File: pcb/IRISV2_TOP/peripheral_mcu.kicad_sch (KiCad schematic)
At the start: 30 parts, among them IC2 S25FL256LAGNFI010, IC3 STM32C552MET6, J6 Conn_02x04_Top_Bottom, Y3 24mHz 8pf, Y4 32.768kHz 12.5pF

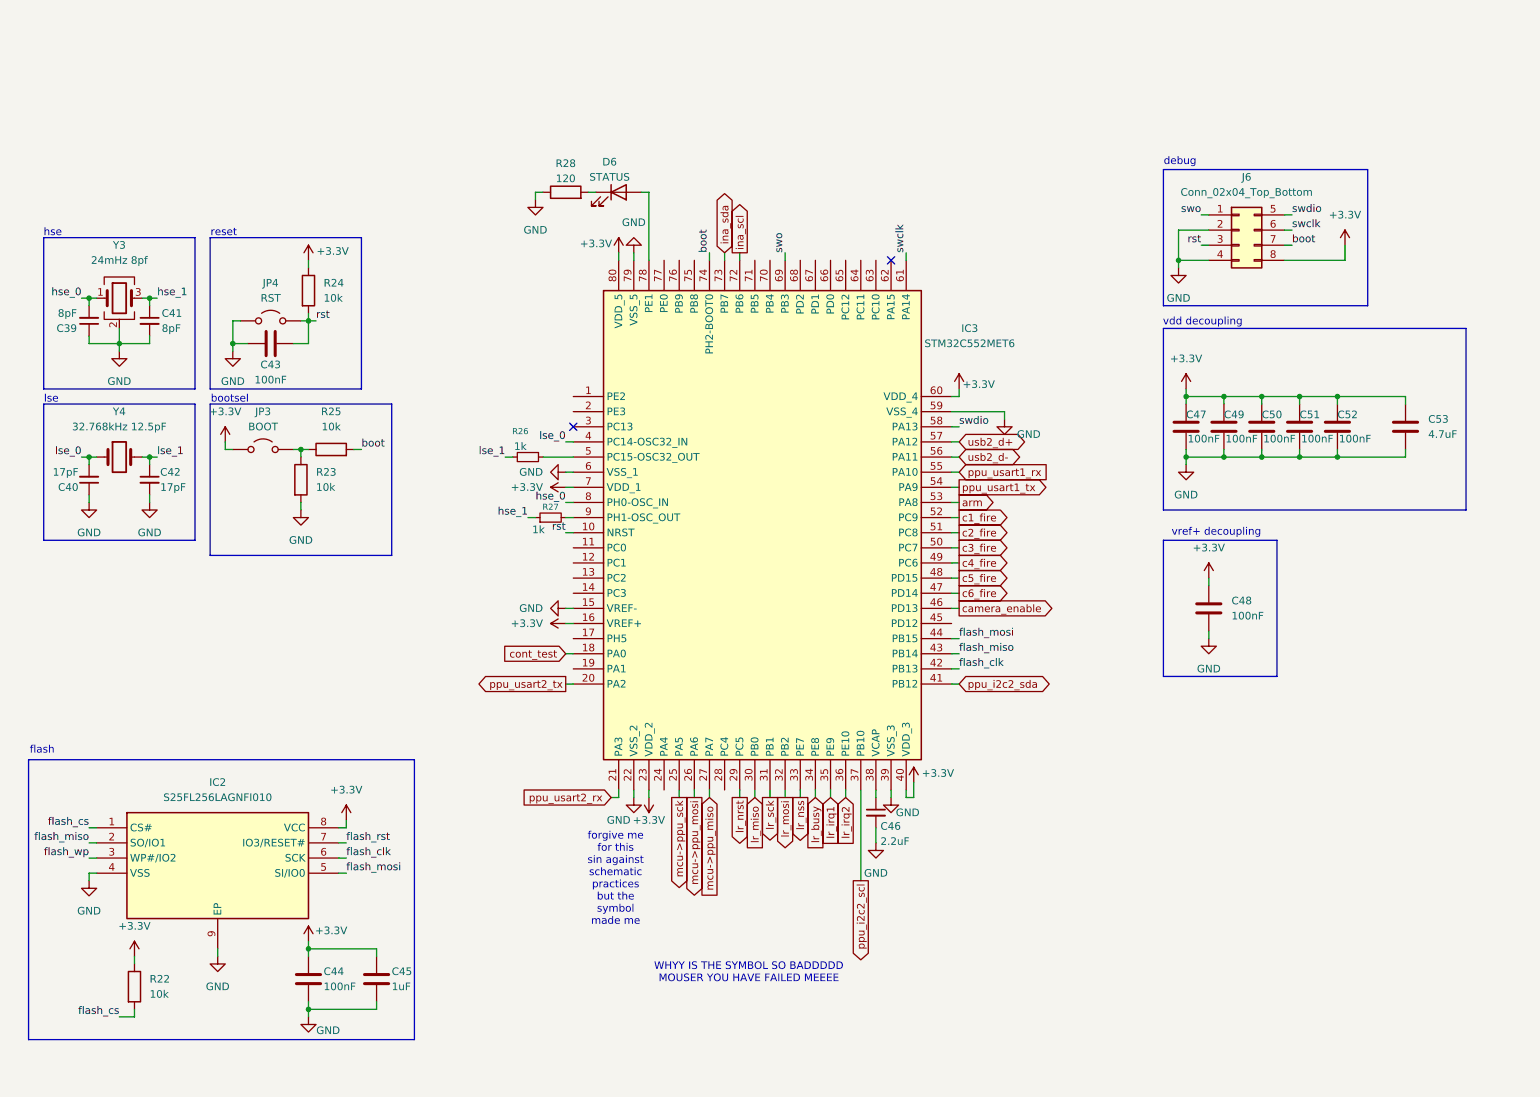
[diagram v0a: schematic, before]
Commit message: split into subprojects, fixed up stuff, started real pcb work
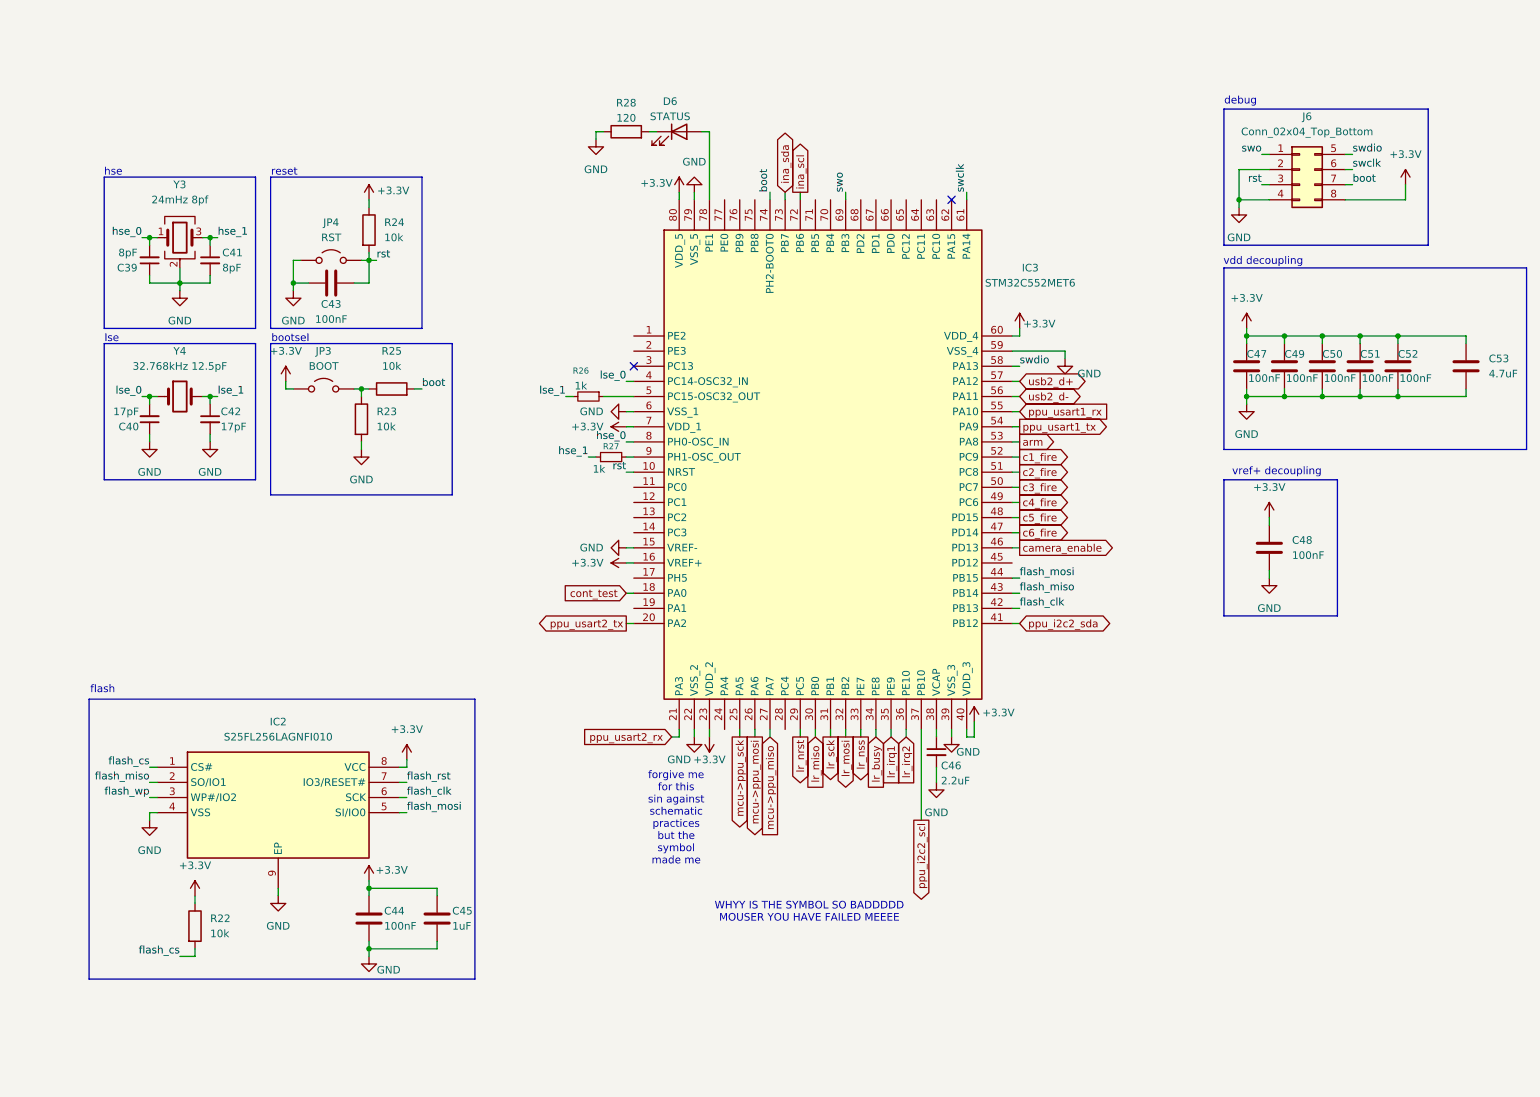
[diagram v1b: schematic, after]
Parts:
- Y3: footprint (none) -> Crystal:Crystal_SMD_3225-4Pin_3.2x2.5mm
- Y4: footprint (none) -> Crystal:Crystal_SMD_3215-2Pin_3.2x1.5mm
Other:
- moved on the sheet: C39, C40, C41, C42, C43, C44, C45, C46, C47, C48, C49, C50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

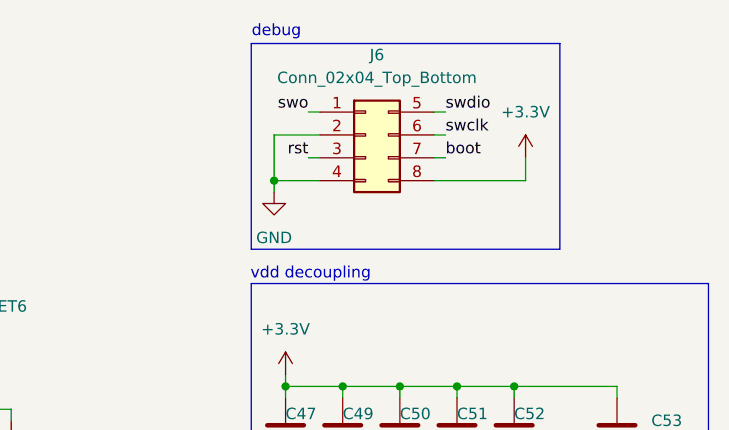
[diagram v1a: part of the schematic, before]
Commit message: gps finished minus tvs (WHY ARE THEY ALL 0201), top layout + routing started
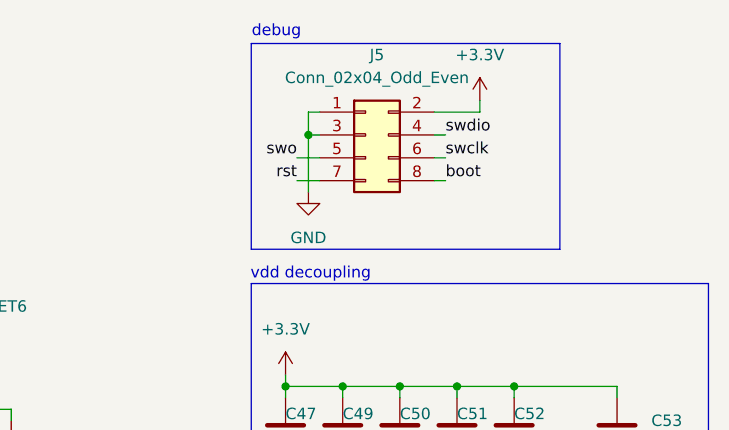
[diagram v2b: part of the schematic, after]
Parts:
- removed J6: Conn_02x04_Top_Bottom, symbol Connector_Generic:Conn_02x04_Top_Bottom
- added J5: Conn_02x04_Odd_Even, Connector_PinHeader_2.54mm:PinHeader_2x04_P2.54mm_Vertical, symbol Connector_Generic:Conn_02x04_Odd_Even
- D6: footprint (none) -> LED_SMD:LED_0805_2012Metric
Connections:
- net +3.3V: now also J5.2 (Pin_2)
- net GND: now also J5.1 (Pin_1), J5.3 (Pin_3)
- net boot: now also J5.8 (Pin_8)
- net rst: now also J5.7 (Pin_7)
- net swclk: now also J5.6 (Pin_6)
- net swdio: now also J5.4 (Pin_4)
- net swo: now also J5.5 (Pin_5)

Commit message: removed high g accel, top board layout looking decent, routing started also - though i realized i was missing the micro sd card and that's going to be a pain to add
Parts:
- removed C43: 100nF, Capacitor_SMD:C_0402_1005Metric, symbol Device:C
- removed JP3: BOOT, TestPoint:TestPoint_2Pads_Pitch2.54mm_Drill0.8mm, symbol Jumper:Jumper_2_Open
- removed JP4: RST, TestPoint:TestPoint_2Pads_Pitch2.54mm_Drill0.8mm, symbol Jumper:Jumper_2_Open
- removed R24: 10k, Resistor_SMD:R_0402_1005Metric, symbol Device:R
- added C1: 100nF, Capacitor_SMD:C_0402_1005Metric, symbol Device:C
- added R5: 10k, Resistor_SMD:R_0402_1005Metric, symbol Device:R
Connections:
- net ppu_i2c2_scl is gone; now on net flash_rst: IC3.37 (PB10)
- net ppu_i2c2_sda is gone; now on net flash_cs: IC3.41 (PB12)
- net +3.3V: now also R5.1
- net GND: now also C1.2
- net flash_wp: now also IC3.45 (PD12)
- net lr_nss: now also IC3.24 (PA4); no longer IC3.33 (PE7)
- net rst: now also C1.1, R5.2
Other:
- moved on the sheet: R23, R25

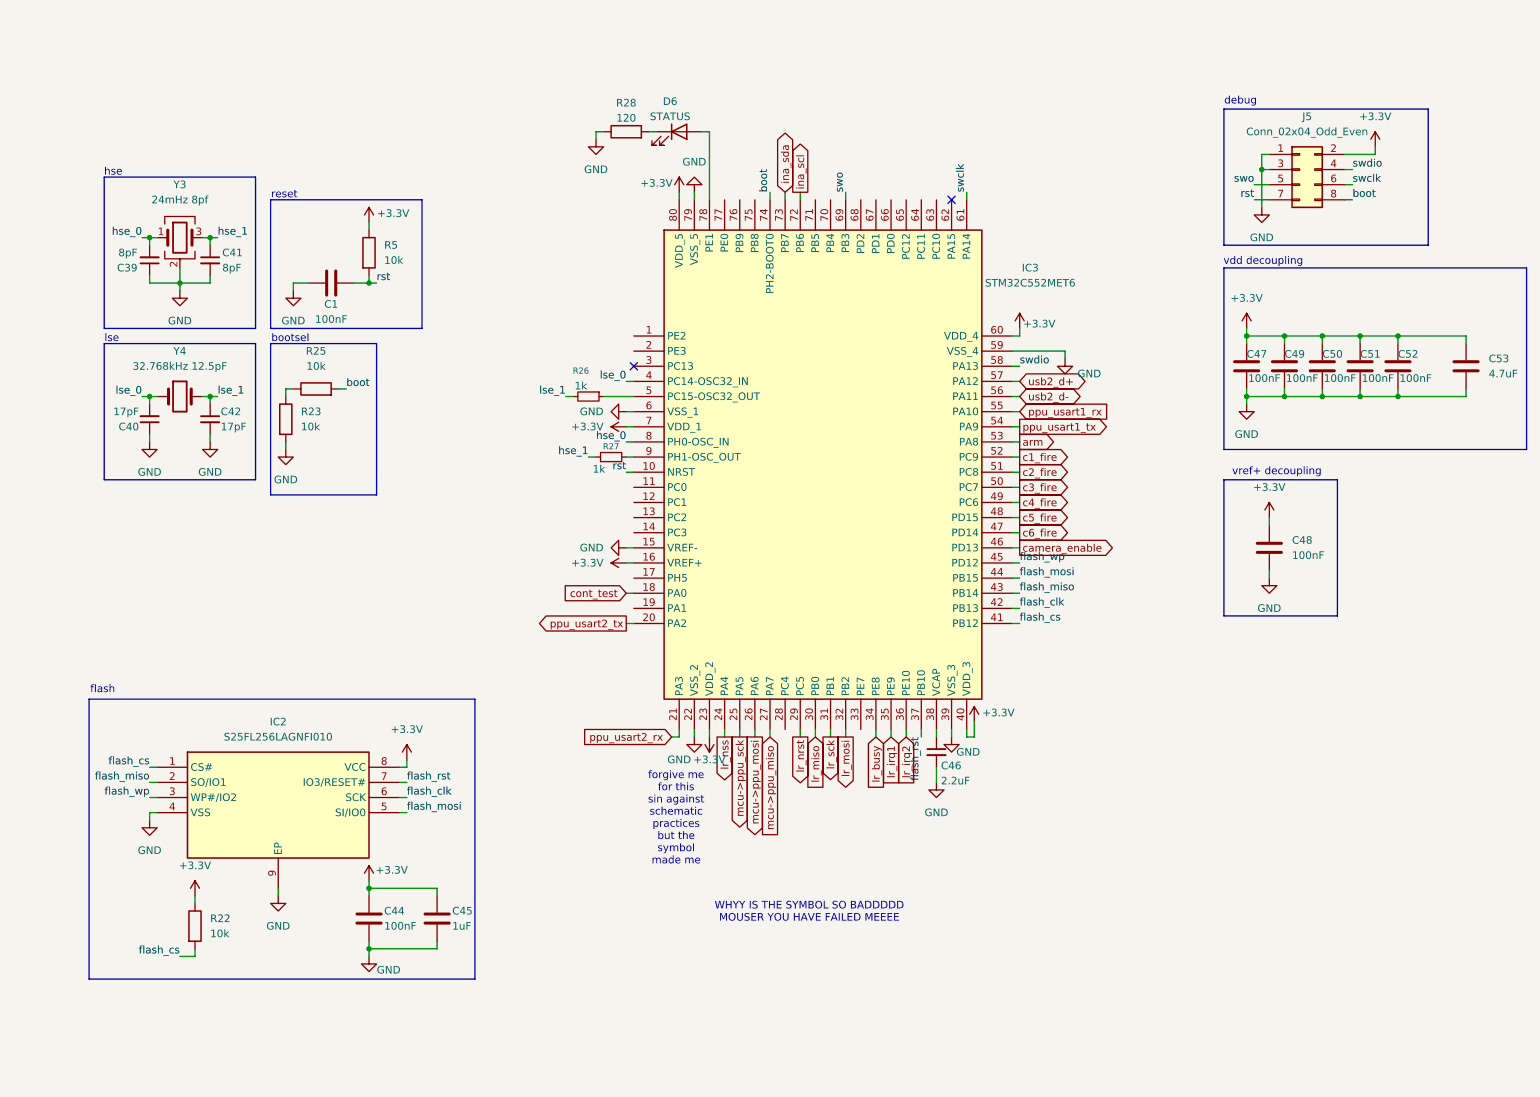
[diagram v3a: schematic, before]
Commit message: layout pretty much done, lr2021 rf stuff done, mostly just routing left
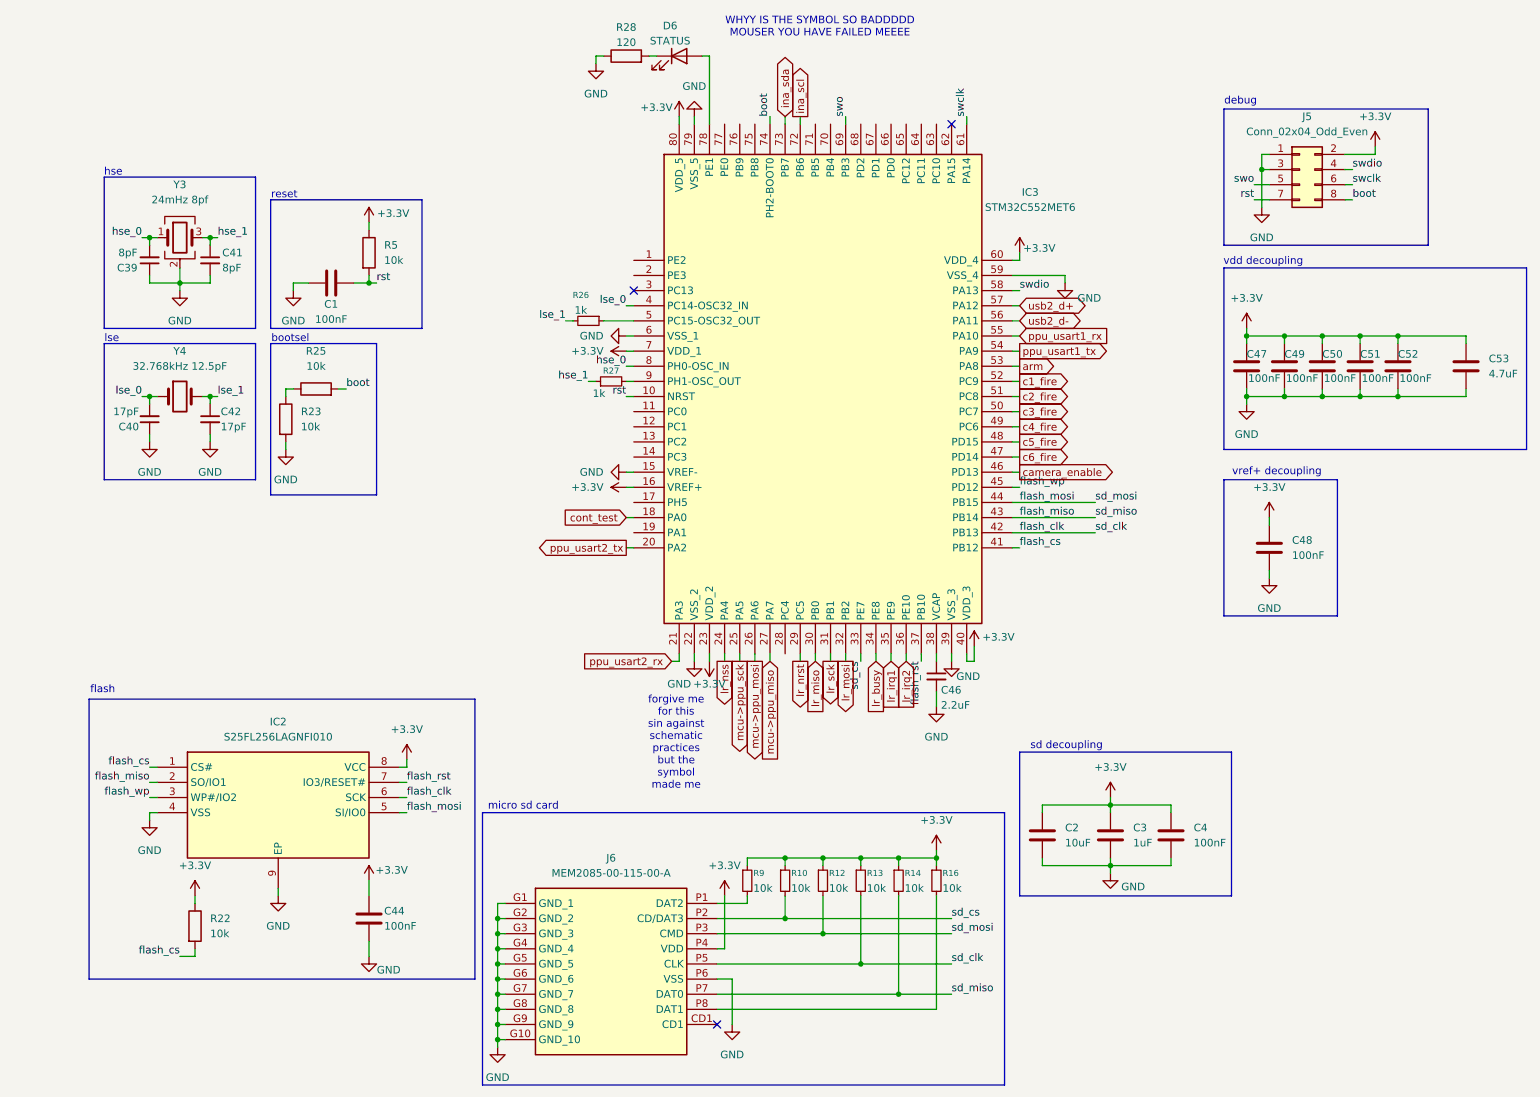
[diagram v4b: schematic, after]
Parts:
- removed C45: 1uF, Capacitor_SMD:C_0603_1608Metric, symbol Device:C
- added C2: 10uF, Capacitor_SMD:C_0603_1608Metric, symbol Device:C
- added C3: 1uF, Capacitor_SMD:C_0603_1608Metric, symbol Device:C
- added C4: 100nF, Capacitor_SMD:C_0402_1005Metric, symbol Device:C
- added J6: MEM2085-00-115-00-A, MEM2085-00-115:MEM20850011500A, symbol MEM2085-00-115-00-A:MEM2085-00-115-00-A
- added R10, R12, R13, R14, R16, R9: 10k, Resistor_SMD:R_0402_1005Metric, symbol Device:R_Small
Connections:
- net +3.3V: now also C2.1, C3.1, C4.1, J6.P4 (VDD), R10.1, R12.1, R13.1, R14.1, R16.1, R9.1
- net GND: now also C2.2, C3.2, C4.2, J6.G1 (GND_1), J6.G10 (GND_10), J6.G2 (GND_2), J6.G3 (GND_3), J6.G4 (GND_4), J6.G5 (GND_5), J6.G6 (GND_6), J6.G7 (GND_7), J6.G8 (GND_8), J6.G9 (GND_9), J6.P6 (VSS)
- net flash_clk: now also J6.P5 (CLK), R13.2
- net flash_miso: now also J6.P7 (DAT0), R14.2
- net flash_mosi: now also J6.P3 (CMD), R12.2
- net sd_cs: now reaches IC3.33 (PE7)
- net sd_cs: now also J6.P2 (CD/DAT3), R10.2
- new net: J6.P8 (DAT1), R16.2
- new net: J6.P1 (DAT2), R9.2
- no-connect marks 2 -> 3
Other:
- note added: "micro sd card"
- note added: "sd decoupling"
- moved on the sheet: C46, D6, IC3, R26, R27, R28
